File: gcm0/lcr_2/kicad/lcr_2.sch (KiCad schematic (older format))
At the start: 128 parts, among them J1 5V, J2 -5V, J3 Conn_01x01_Male, J4 Conn_01x03_Male, J5 Conn_01x01_Male, J6 Conn_01x01_Male, J8 SWD, Q1 BC547, Q2 BC547, Q3 BC547, SW1 1, SW2 2, U1 RC4580, U10 RC4580, U11 74HC595, U12 STM32F030F4P6, U2 74HC4053PW,112, U3 74HC4052PW,118, U4 RC4580, U5 LM2596S-5, U6 LM7805_TO220, U7 RC4580, U8 LM1117-3.3, U9 74HC4053PW,112, Y1 8M

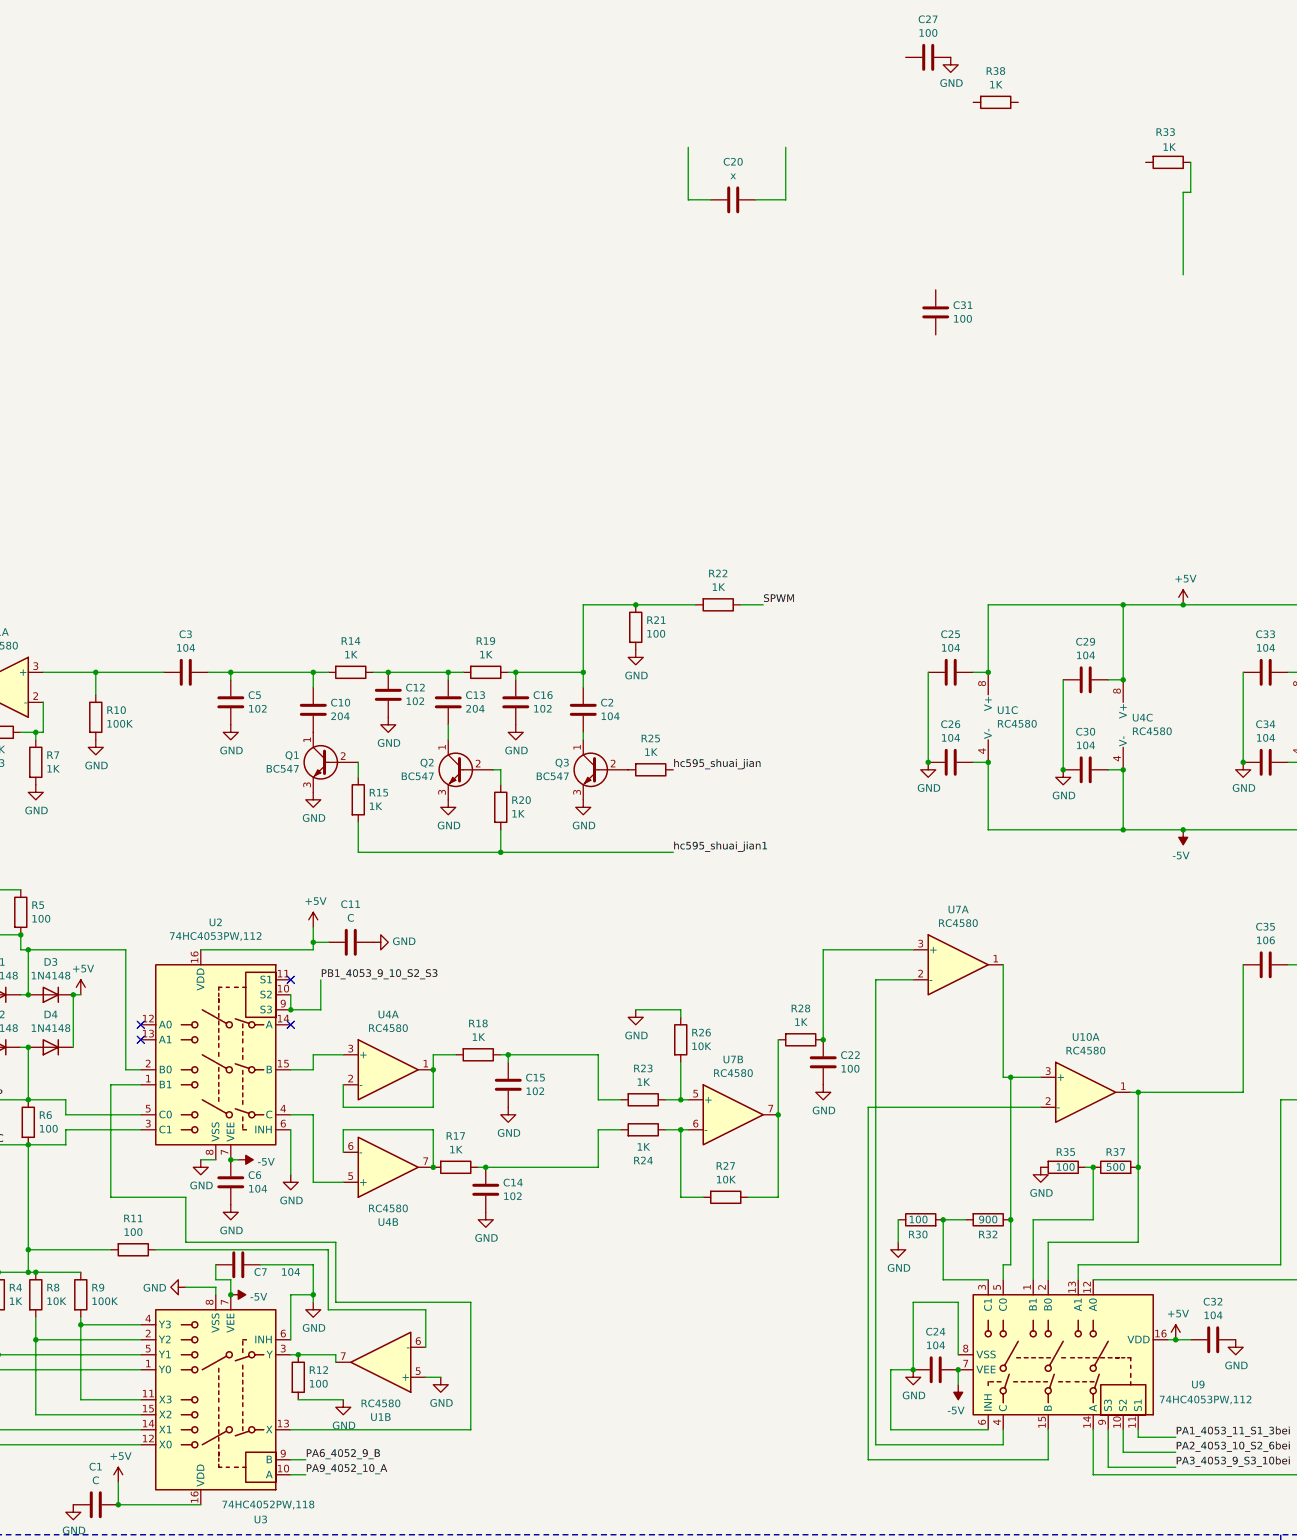
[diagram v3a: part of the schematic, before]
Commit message: 电路改错
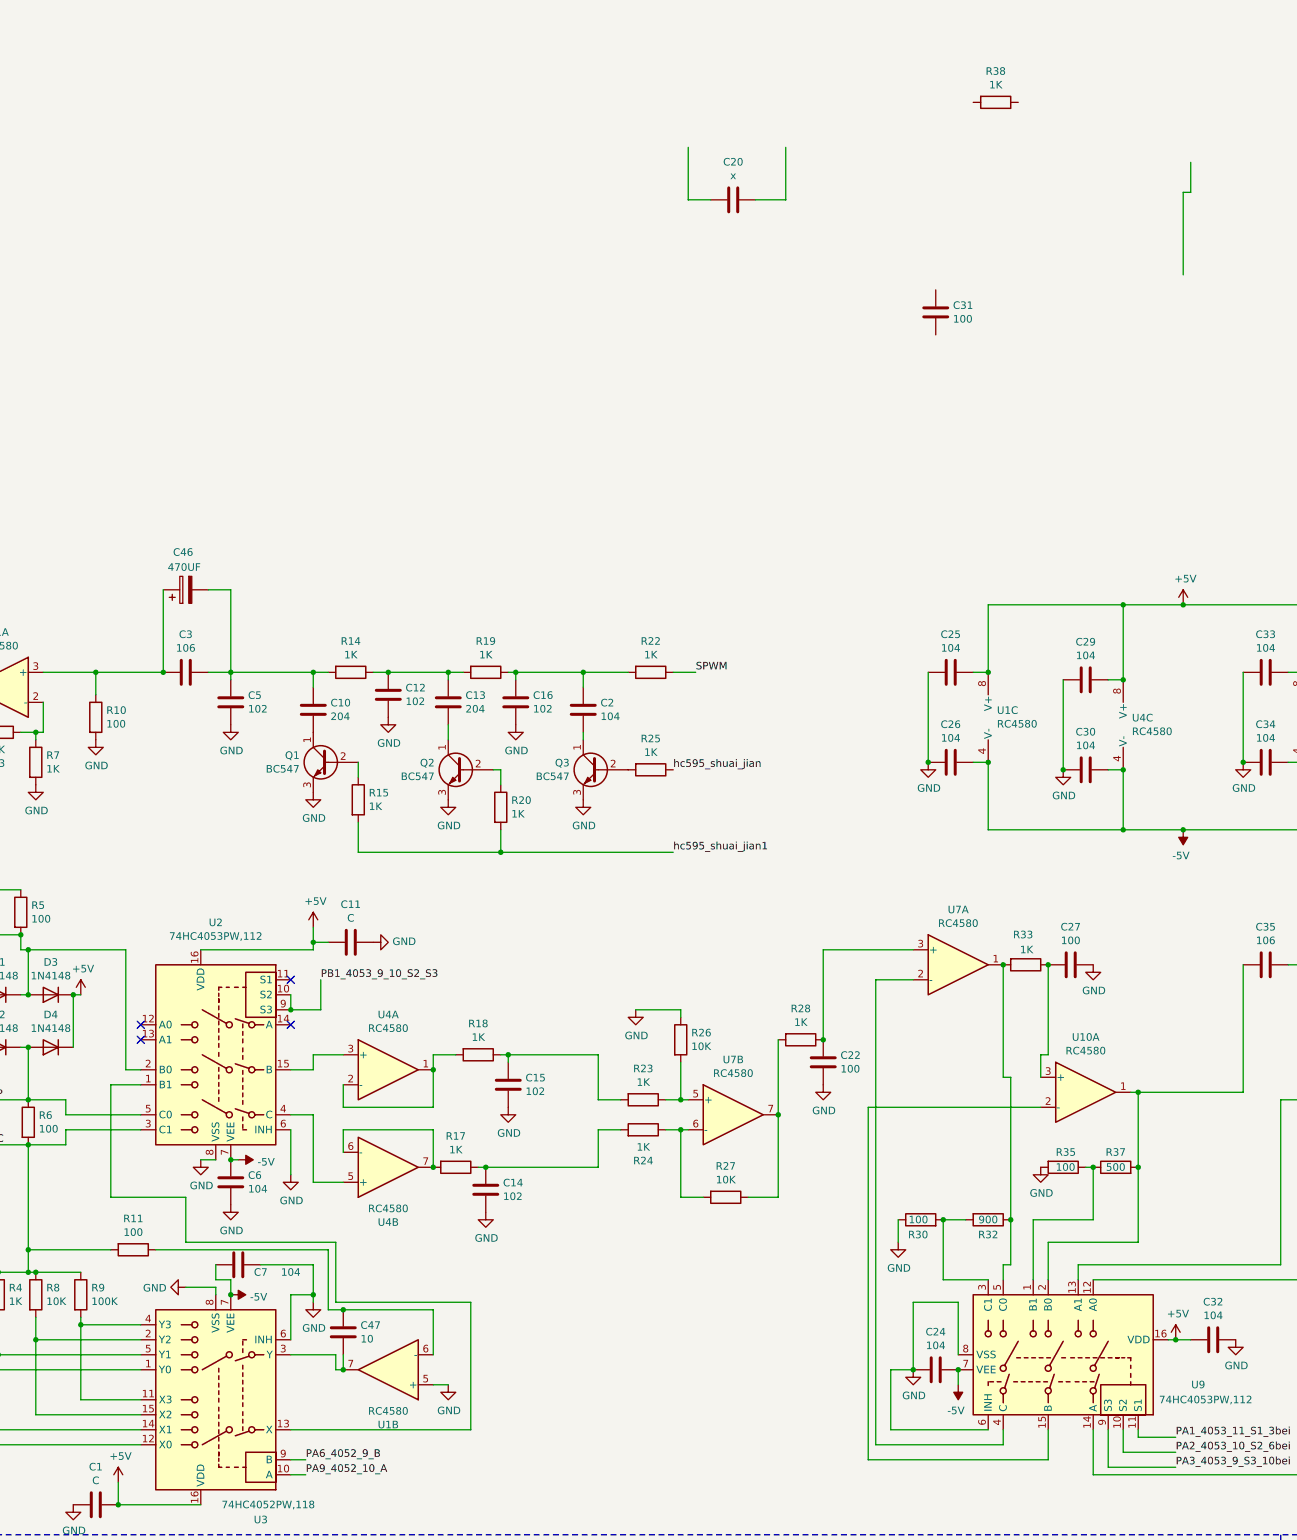
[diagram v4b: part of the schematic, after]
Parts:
- removed R12, R21: 100, Resistor_THT:R_Axial_DIN0204_L3.6mm_D1.6mm_P1.90mm_Vertical, symbol Device:R
- added C46: 470UF, Capacitor_THT:CP_Radial_D8.0mm_P3.80mm, symbol Device:CP
- added C47: 10, symbol Device:C
- C3: value 104 -> 106
- R10: value 100K -> 100
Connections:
- net at C3.2, R10.1, U1.3 (+): now also C46.1
- net at R11.1, U1.6 (-): now also C47.1
- net at U1.7, U3.3 (Y): now also C47.2
- net at C10.1, C3.1, C5.1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: now also C46.2
- net at R32.1, U7.1, U9.5 (C0): now also R33.2; no longer U10.3 (+)
- net at R33.1: now also C27.2, U10.3 (+)
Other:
- moved on the sheet: C27, R22, R33, U1B
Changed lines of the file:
@@
 	5400 8750 5100 8750
 $Comp
-L Amplifier_Operational:RC4580 U1
-U 2 1 61BC6219
-P 3650 6150
-F 0 "U1" H 3650 6517 50  0000 C CNN
-F 1 "RC4580" H 3650 6426 50  0000 C CNN
-F 2 "Package_SO:SOP-8_3.9x4.9mm_P1.27mm" H 3650 6150 50  0001 C CNN
-F 3 "http://www.ti.com/lit/ds/symlink/rc4580.pdf" H 3650 6150 50  0001 C CNN
-	2    3650 6150
-	-1   0    0    1
-$EndComp
-$Comp
 L Device:C C3
 U 1 1 61C2DF21
 P 2350 1550
 F 0 "C3" V 2098 1550 50  0000 C CNN
-F 1 "104" V 2189 1550 50  0000 C CNN
+F 1 "106" V 2189 1550 50  0000 C CNN
 F 2 "Capacitor_SMD:C_0805_2012Metric_Pad1.18x1.45mm_HandSolder" H 2388 1400 50  0001 C CNN
 F 3 "~" H 2350 1550 50  0001 C CNN
@@
 	5000 1950 5000 2000
 $Comp
-L Analog_Switch:CD4052B U3
-U 1 1 61C7CE8E
-P 2550 6400
-F 0 "U3" H 2250 7200 50  0000 C CNN
-F 1 "74HC4052PW,118" H 2200 7100 50  0000 C CNN
-F 2 "Package_SO:TSSOP-16_4.4x5mm_P0.65mm" H 2700 5650 50  0001 L CNN
-F 3 "" H 2530 6600 50  0001 C CNN
-	1    2550 6400
-	-1   0    0    1
-$EndComp
-$Comp
 L Analog_Switch:CD4053B U2
 U 1 1 61C9E43B
@@
 	1650 5850 1650 5900
 Wire Wire Line
-	1650 5900 2050 5900
-Wire Wire Line
 	1100 5850 1100 6100
 Wire Wire Line
-	1100 6100 2050 6100
-Wire Wire Line
 	800  5850 800  6200
 Wire Wire Line
-	800  6200 2050 6200
-Wire Wire Line
-	2050 6400 1650 6400
-Wire Wire Line
 	1650 6400 1650 5900
 Connection ~ 1650 5900
 Wire Wire Line
-	2050 6600 1100 6600
-Wire Wire Line
 	1100 6600 1100 6100
 Connection ~ 1100 6100
 Wire Wire Line
-	2050 6700 800  6700
-Wire Wire Line
 	800  6700 800  6200
 Connection ~ 800  6200
@@
 	3500 2750 4450 2750
 Connection ~ 4450 2750
-Text Label 6200 1100 0    50   ~ 0
+Text Label 5750 1550 0    50   ~ 0
 SPWM
 $Comp
@@
 Wire Wire Line
 	1350 5850 1350 6000
-Wire Wire Line
-	1350 6500 2050 6500
-Wire Wire Line
-	2050 6000 1350 6000
 Connection ~ 1350 6000
 Wire Wire Line
@@
 L Device:R R22
 U 1 1 625D8345
-P 5900 1100
-F 0 "R22" V 5693 1100 50  0000 C CNN
-F 1 "1K" V 5784 1100 50  0000 C CNN
-F 2 "Resistor_THT:R_Axial_DIN0204_L3.6mm_D1.6mm_P1.90mm_Vertical" V 5830 1100 50  0001 C CNN
-F 3 "~" H 5900 1100 50  0001 C CNN
-	1    5900 1100
+P 5450 1550
+F 0 "R22" V 5243 1550 50  0000 C CNN
+F 1 "1K" V 5334 1550 50  0000 C CNN
+F 2 "Resistor_THT:R_Axial_DIN0204_L3.6mm_D1.6mm_P1.90mm_Vertical" V 5380 1550 50  0001 C CNN
+F 3 "~" H 5450 1550 50  0001 C CNN
+	1    5450 1550
 	0    1    1    0
 $EndComp
-Connection ~ 5000 1550
 Wire Wire Line
-	6050 1100 6200 1100
+	5600 1550 5750 1550
 Wire Wire Line
 	3700 1550 4100 1550
@@
 P 1750 1850
 F 0 "R10" H 1820 1896 50  0000 L CNN
-F 1 "100K" H 1820 1805 50  0000 L CNN
+F 1 "100" H 1820 1805 50  0000 L CNN
 F 2 "Resistor_THT:R_Axial_DIN0204_L3.6mm_D1.6mm_P1.90mm_Vertical" V 1680 1850 50  0001 C CNN
 F 3 "~" H 1750 1850 50  0001 C CNN
@@
 L power:GND #PWR024
 U 1 1 61CF692E
-P 4050 6250
-F 0 "#PWR024" H 4050 6000 50  0001 C CNN
-F 1 "GND" H 4055 6077 50  0000 C CNN
-F 2 "" H 4050 6250 50  0001 C CNN
-F 3 "" H 4050 6250 50  0001 C CNN
-	1    4050 6250
+P 4100 6300
+F 0 "#PWR024" H 4100 6050 50  0001 C CNN
+F 1 "GND" H 4105 6127 50  0000 C CNN
+F 2 "" H 4100 6300 50  0001 C CNN
+F 3 "" H 4100 6300 50  0001 C CNN
+	1    4100 6300
 	1    0    0    -1
 $EndComp
 Wire Wire Line
-	3950 6250 4050 6250
-Wire Wire Line
-	3950 5800 3950 6050
-Wire Wire Line
-	3300 5800 3950 5800
+	4000 6300 4100 6300
 Wire Wire Line
 	3350 5750 4250 5750
@@
 	3050 6600 4250 6600
 Wire Wire Line
-	3050 6100 3100 6100
-Wire Wire Line
-	3350 6100 3350 6150
-$Comp
-L power:GND #PWR021
-U 1 1 61E789F5
-P 3400 6400
-F 0 "#PWR021" H 3400 6150 50  0001 C CNN
-F 1 "GND" H 3405 6227 50  0000 C CNN
-F 2 "" H 3400 6400 50  0001 C CNN
-F 3 "" H 3400 6400 50  0001 C CNN
-	1    3400 6400
-	1    0    0    -1
-$EndComp
-$Comp
-L Device:R R12
-U 1 1 61E7A756
-P 3100 6250
-F 0 "R12" H 3170 6296 50  0000 L CNN
-F 1 "100" H 3170 6205 50  0000 L CNN
-F 2 "Resistor_THT:R_Axial_DIN0204_L3.6mm_D1.6mm_P1.90mm_Vertical" V 3030 6250 50  0001 C CNN
-F 3 "~" H 3100 6250 50  0001 C CNN
-	1    3100 6250
-	1    0    0    -1
-$EndComp
-Connection ~ 3100 6100
-Wire Wire Line
-	3100 6100 3350 6100
-Wire Wire Line
-	3100 6400 3400 6400
-Wire Wire Line
 	4000 4600 4000 4850
 $Comp
@@
 	1    0    0    -1
 $EndComp
-Wire Wire Line
-	1900 7100 2450 7100
 Connection ~ 1900 7100
 Wire Wire Line
@@
 	0    1    1    0
 $EndComp
-Connection ~ 2650 5700
 $Comp
 L Device:C C11
@@
 L Device:C C27
 U 1 1 632A707B
-P 7300 -2550
-F 0 "C27" V 7048 -2550 50  0000 C CNN
-F 1 "100" V 7139 -2550 50  0000 C CNN
-F 2 "Capacitor_SMD:C_0603_1608Metric_Pad1.08x0.95mm_HandSolder" H 7338 -2700 50  0001 C CNN
-F 3 "~" H 7300 -2550 50  0001 C CNN
-	1    7300 -2550
+P 8250 3500
+F 0 "C27" V 7998 3500 50  0000 C CNN
+F 1 "100" V 8089 3500 50  0000 C CNN
+F 2 "Capacitor_SMD:C_0603_1608Metric_Pad1.08x0.95mm_HandSolder" H 8288 3350 50  0001 C CNN
+F 3 "~" H 8250 3500 50  0001 C CNN
+	1    8250 3500
 	0    1    1    0
 $EndComp
@@
 L power:GND #PWR039
 U 1 1 632AA5CA
-P 7450 -2550
-F 0 "#PWR039" H 7450 -2800 50  0001 C CNN
-F 1 "GND" H 7455 -2723 50  0000 C CNN
-F 2 "" H 7450 -2550 50  0001 C CNN
-F 3 "" H 7450 -2550 50  0001 C CNN
-	1    7450 -2550
+P 8400 3500
+F 0 "#PWR039" H 8400 3250 50  0001 C CNN
+F 1 "GND" H 8405 3327 50  0000 C CNN
+F 2 "" H 8400 3500 50  0001 C CNN
+F 3 "" H 8400 3500 50  0001 C CNN
+	1    8400 3500
 	1    0    0    -1
 $EndComp
@@
 L Device:R R33
 U 1 1 632A4B7C
-P 8900 -1850
-F 0 "R33" V 8700 -1800 50  0000 R CNN
-F 1 "1K" V 8800 -1800 50  0000 R CNN
-F 2 "Resistor_THT:R_Axial_DIN0204_L3.6mm_D1.6mm_P1.90mm_Vertical" V 8830 -1850 50  0001 C CNN
-F 3 "~" H 8900 -1850 50  0001 C CNN
-	1    8900 -1850
+P 7950 3500
+F 0 "R33" V 7750 3550 50  0000 R CNN
+F 1 "1K" V 7850 3550 50  0000 R CNN
+F 2 "Resistor_THT:R_Axial_DIN0204_L3.6mm_D1.6mm_P1.90mm_Vertical" V 7880 3500 50  0001 C CNN
+F 3 "~" H 7950 3500 50  0001 C CNN
+	1    7950 3500
 	0    1    1    0
 $EndComp
@@
 	0    1    1    0
 $EndComp
-Wire Wire Line
-	5750 1100 5350 1100
-Wire Wire Line
-	5000 1100 5000 1550
-$Comp
-L Device:R R21
-U 1 1 61E47858
-P 5350 1250
-F 0 "R21" H 5420 1296 50  0000 L CNN
-F 1 "100" H 5420 1205 50  0000 L CNN
-F 2 "Resistor_THT:R_Axial_DIN0204_L3.6mm_D1.6mm_P1.90mm_Vertical" V 5280 1250 50  0001 C CNN
-F 3 "~" H 5350 1250 50  0001 C CNN
-	1    5350 1250
-	1    0    0    -1
-$EndComp
-Connection ~ 5350 1100
-Wire Wire Line
-	5350 1100 5000 1100
-$Comp
-L power:GND #PWR09
-U 1 1 61F0040F
-P 5350 1400
-F 0 "#PWR09" H 5350 1150 50  0001 C CNN
-F 1 "GND" H 5355 1227 50  0000 C CNN
-F 2 "" H 5350 1400 50  0001 C CNN
-F 3 "" H 5350 1400 50  0001 C CNN
-	1    5350 1400
-	1    0    0    -1
-$EndComp
 $Comp
 L power:GND #PWR035
@@
 	8000 5200 8000 5600
 Connection ~ 8400 4850
+Connection ~ 7800 3500
+Wire Wire Line
+	8100 3500 8100 4100
+Wire Wire Line
+	8100 4100 8050 4100
+Wire Wire Line
+	8050 4100 8050 4250
+Connection ~ 8100 3500
+Wire Wire Line
+	5300 1550 5000 1550
+Connection ~ 5000 1550
+$Comp
+L Device:CP C46
+U 1 1 620E9A56
+P 2350 1000
+F 0 "C46" V 2600 950 50  0000 L CNN
+F 1 "470UF" V 2500 900 50  0000 L CNN
+F 2 "Capacitor_THT:CP_Radial_D8.0mm_P3.80mm" H 2388 850 50  0001 C CNN
+F 3 "~" H 2350 1000 50  0001 C CNN
+	1    2350 1000
+	0    -1   -1   0
+$EndComp
+Wire Wire Line
+	2500 1000 2650 1000
+Wire Wire Line
+	2650 1000 2650 1550
+Wire Wire Line
+	2200 1000 2200 1550
+Connection ~ 2200 1550
+Connection ~ 2650 5700
+Wire Wire Line
+	1900 7100 2450 7100
+Wire Wire Line
+	2050 6700 800  6700
+Wire Wire Line
+	2050 6600 1100 6600
+Wire Wire Line
+	1350 6500 2050 6500
+Wire Wire Line
+	2050 6400 1650 6400
+Wire Wire Line
+	800  6200 2050 6200
+Wire Wire Line
+	1100 6100 2050 6100
+Wire Wire Line
+	2050 6000 1350 6000
+Wire Wire Line
+	1650 5900 2050 5900
+$Comp
+L Analog_Switch:CD4052B U3
+U 1 1 61C7CE8E
+P 2550 6400
+F 0 "U3" H 2250 7200 50  0000 C CNN
+F 1 "74HC4052PW,118" H 2200 7100 50  0000 C CNN
+F 2 "Package_SO:TSSOP-16_4.4x5mm_P0.65mm" H 2700 5650 50  0001 L CNN
+F 3 "" H 2530 6600 50  0001 C CNN
+	1    2550 6400
+	-1   0    0    1
+$EndComp
+$Comp
+L Amplifier_Operational:RC4580 U1
+U 2 1 61BC6219
+P 3700 6200
+F 0 "U1" H 3700 6567 50  0000 C CNN
+F 1 "RC4580" H 3700 6476 50  0000 C CNN
+F 2 "Package_SO:SOP-8_3.9x4.9mm_P1.27mm" H 3700 6200 50  0001 C CNN
+F 3 "http://www.ti.com/lit/ds/symlink/rc4580.pdf" H 3700 6200 50  0001 C CNN
+	2    3700 6200
+	-1   0    0    1
+$EndComp
+Wire Wire Line
+	3050 6100 3350 6100
+Wire Wire Line
+	3300 5800 3400 5800
+Wire Wire Line
+	3350 6200 3400 6200
+Wire Wire Line
+	3350 6100 3350 6200
+$Comp
+L Device:C C47
+U 1 1 61FE214B
+P 3400 5950
+F 0 "C47" H 3515 5996 50  0000 L CNN
+F 1 "10" H 3515 5905 50  0000 L CNN
+F 2 "" H 3438 5800 50  0001 C CNN
+F 3 "~" H 3400 5950 50  0001 C CNN
+	1    3400 5950
+	1    0    0    -1
+$EndComp
+Connection ~ 3400 5800
+Wire Wire Line
+	4000 6100 4000 5800
+Wire Wire Line
+	3400 5800 4000 5800
 Wire Wire Line
-	8050 4250 7850 4250
-Connection ~ 7850 4250
+	3400 6100 3400 6200
+Connection ~ 3400 6200
 $EndSCHEMATC
